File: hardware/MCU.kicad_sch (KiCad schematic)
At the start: 0 parts

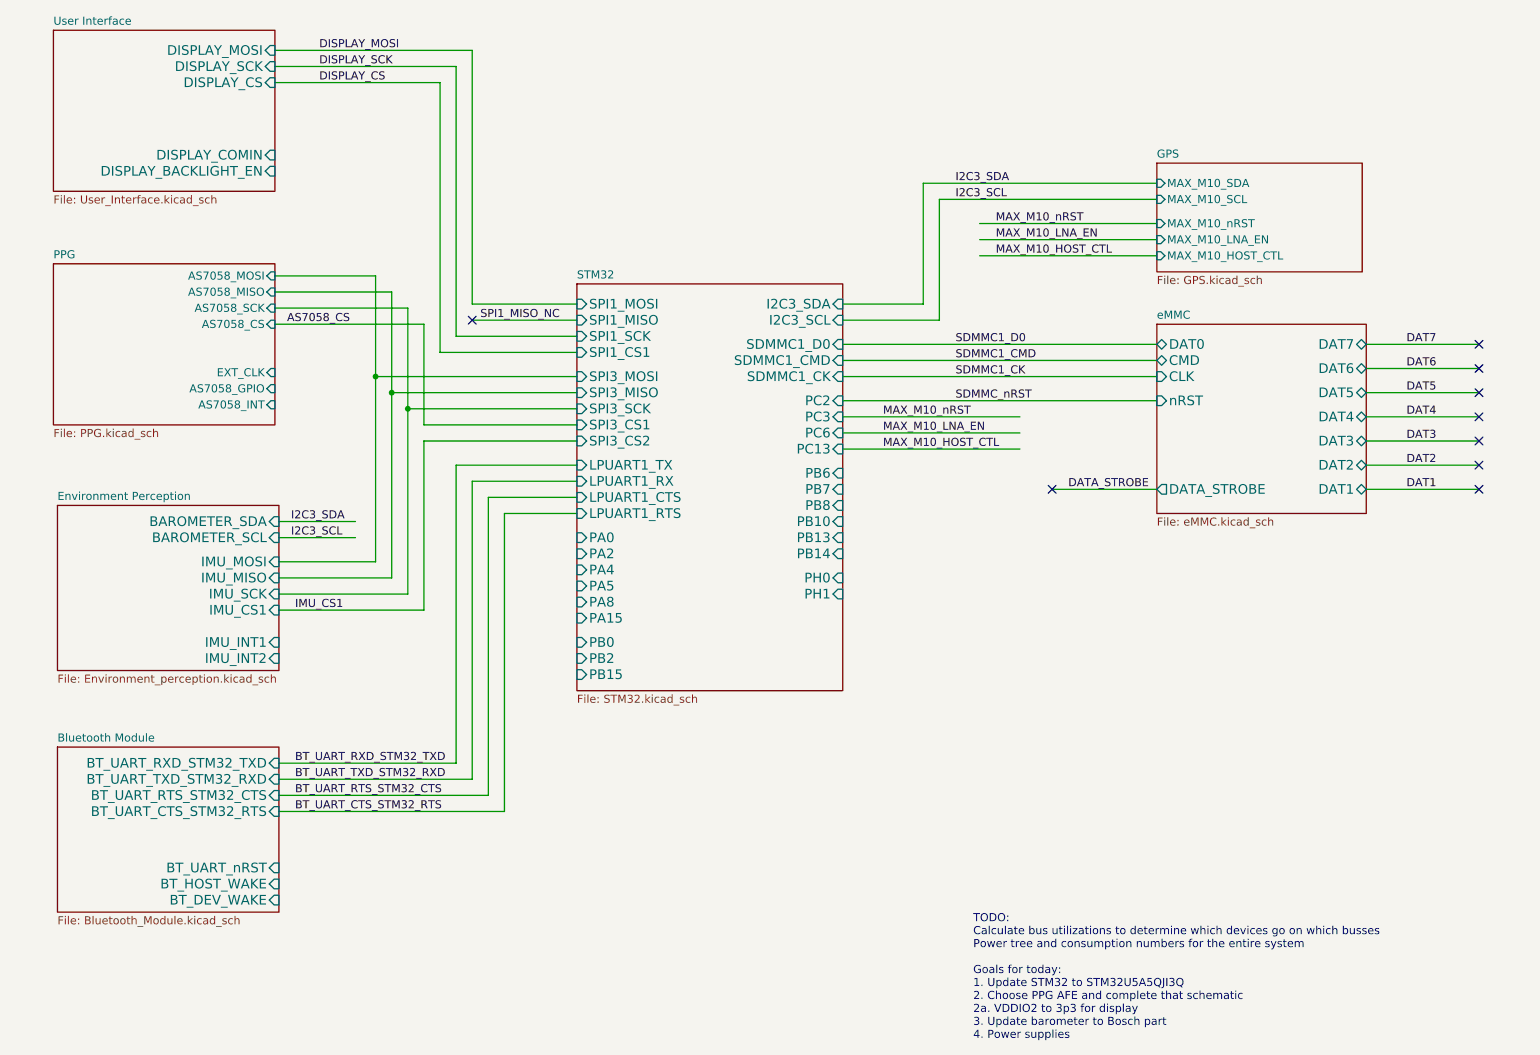
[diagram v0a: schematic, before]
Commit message: Added bosch barometer
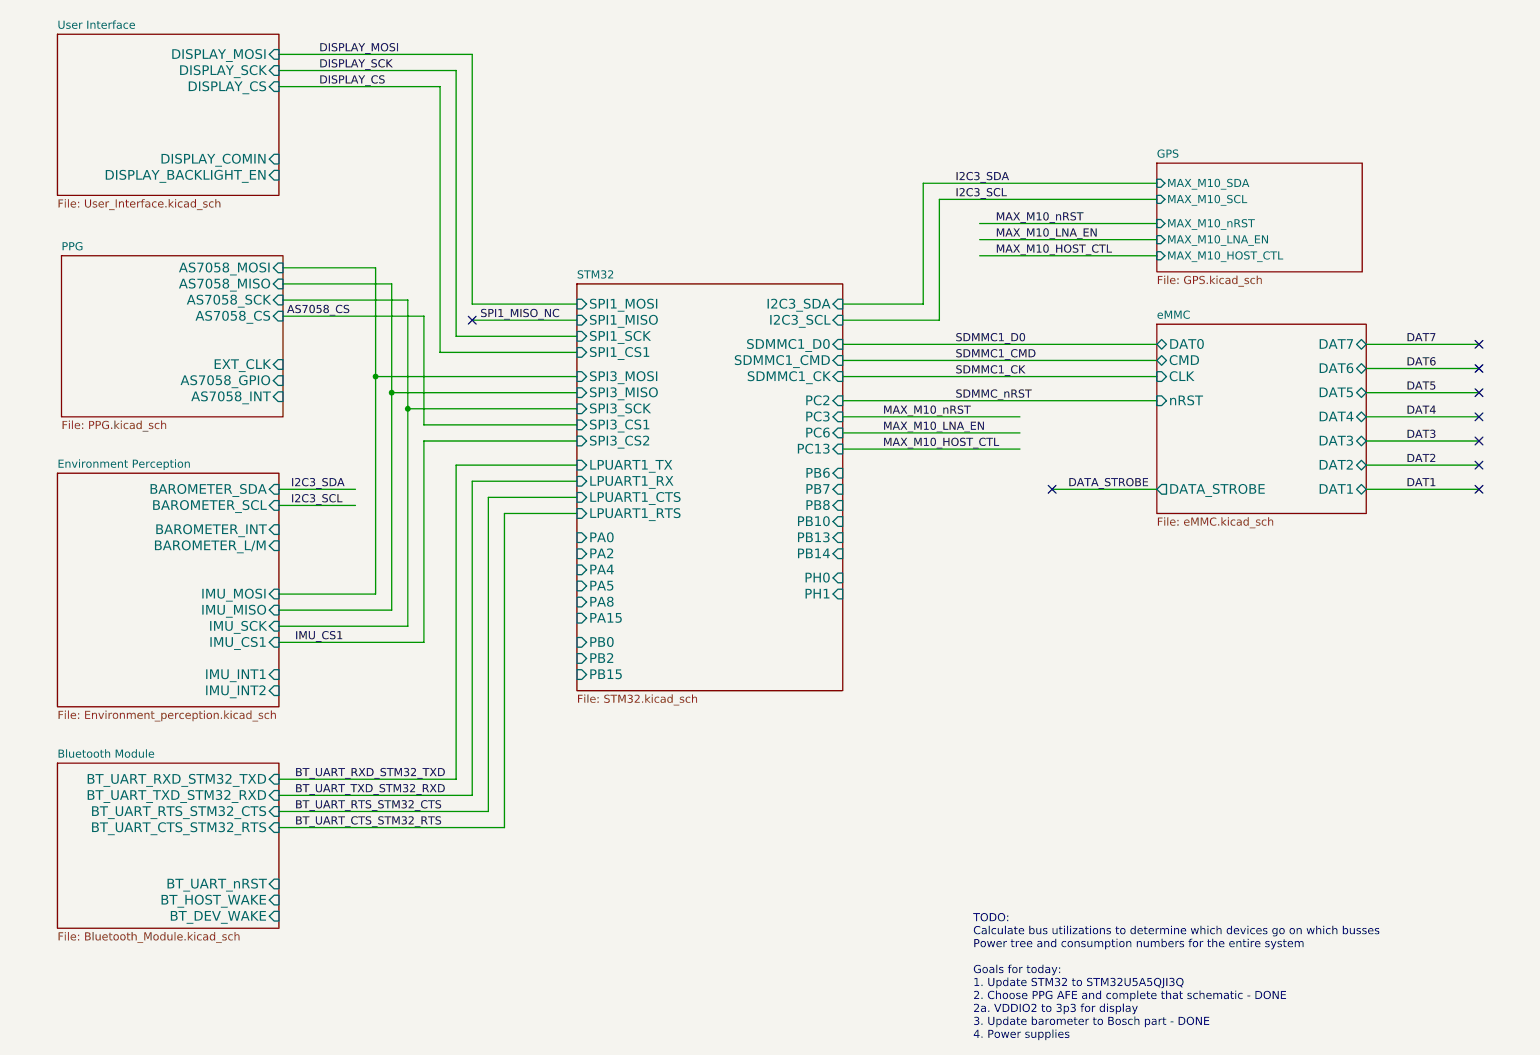
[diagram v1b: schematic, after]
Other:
- sheet Environment Perception ports: added BAROMETER_INT, BAROMETER_L/M; removed none
- note added: "TODO: Calculate bus utilizations to determine which devices go on which busses Power tree and consumption numbers for the entire system Goals for today: 1. Update STM32 to STM32U5A5QJI3Q 2. Choose PPG AFE and complete that schematic - DONE 2a. VDDIO2 to 3p3 for display 3. Update barometer to Bosch part - DONE 4. Power supplies"
- note removed: "TODO: Calculate bus utilizations to determine which devices go on which busses Power tree and consumption numbers for the entire system Goals for today: 1. Update STM32 to STM32U5A5QJI3Q 2. Choose PPG AFE and complete that schematic 2a. VDDIO2 to 3p3 for display 3. Update barometer to Bosch part 4. Power supplies"

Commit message: Contemplating switching back to the 64LQFP
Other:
- note added: "TODO: Calculate bus utilizations to determine which devices go on which busses Power tree and consumption numbers for the entire system - DONE Goals for today: 1. Update STM32 to STM32U5A5QJI3Q 2. Choose PPG AFE and complete that schematic - DONE 2a. VDDIO2 to 3p3 for display 3. Update barometer to Bosch part - DONE 4. Power supplies 5. Add test points to all blocks 6. Fill in actual components 7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"
- note removed: "TODO: Calculate bus utilizations to determine which devices go on which busses Power tree and consumption numbers for the entire system Goals for today: 1. Update STM32 to STM32U5A5QJI3Q 2. Choose PPG AFE and complete that schematic - DONE 2a. VDDIO2 to 3p3 for display 3. Update barometer to Bosch part - DONE 4. Power supplies"
